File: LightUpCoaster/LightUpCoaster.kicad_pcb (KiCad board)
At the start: 2 copper layers, 53 x 61.3 mm, 54 parts, among them Q101 2N7002, Q102 BSS84, Q103 IRLML6244, Q201 2N2222, Q202 2N2222, Q401 IRLML6244, Q402 IRLML6244, Q403 IRLML6244, Q501 IRLML6244, Q601 IRLML6244, SW102 SW_SPDT, SW103 SW_DIP_x01, U103 CR2032, U104 NE555D, U105 4017

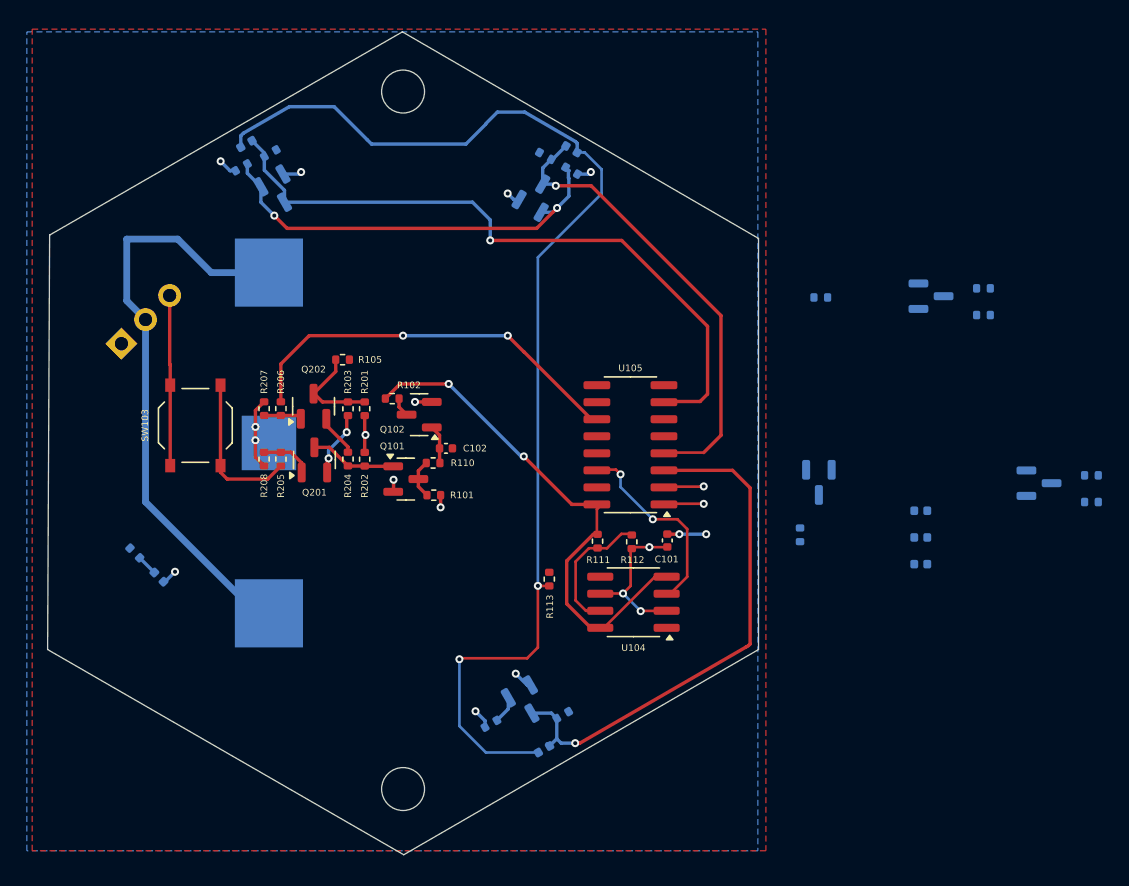
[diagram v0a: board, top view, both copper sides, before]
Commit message: Fixed LED positions
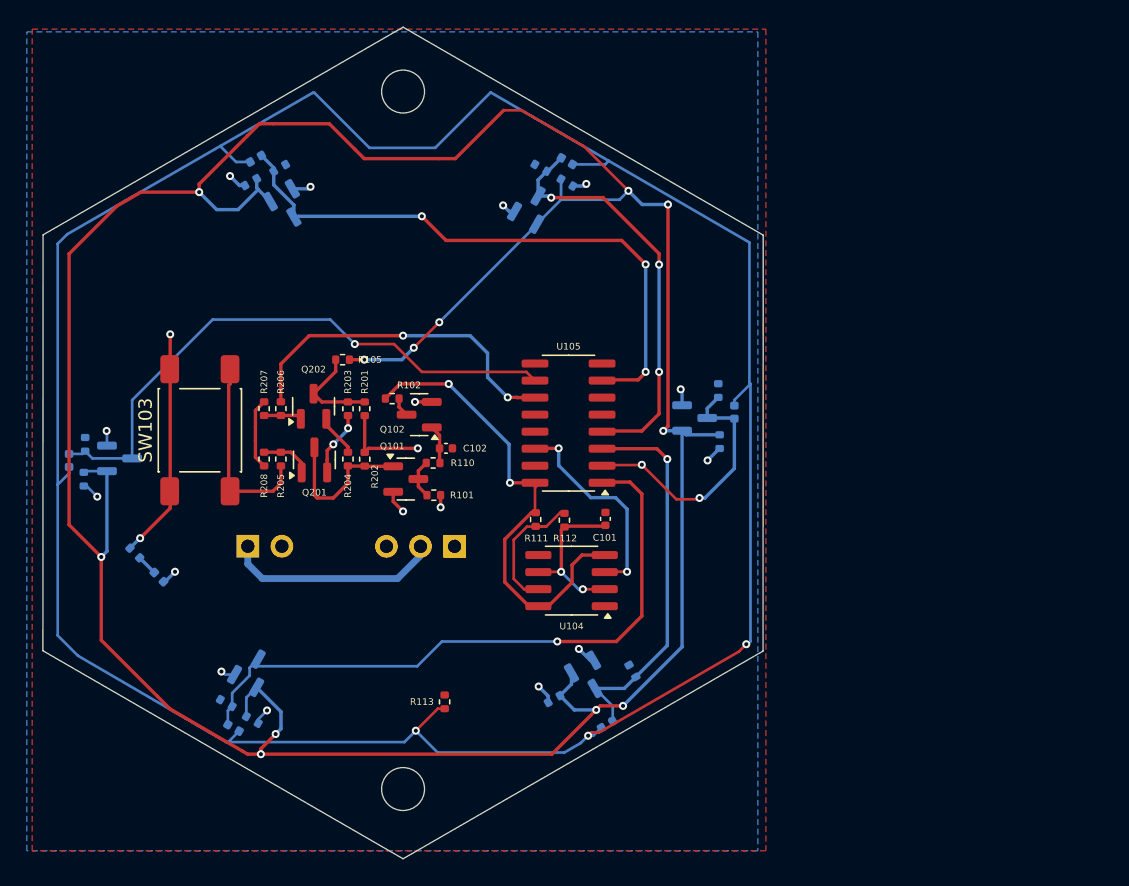
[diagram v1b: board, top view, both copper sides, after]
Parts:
- removed U103: CR2032, Battery_Holder:CR2032-SMD
- added J101: Conn_01x02, Connector_PinHeader_2.54mm:PinHeader_1x02_P2.54mm_Vertical, B.Cu at (138.4, 107.7)
- SW103: footprint Button_Switch_SMD:SW_Push_1P1T_XKB_TS-1187A -> Button_Switch_SMD:SW_Push_1P1T_NO_E-Switch_TL3301NxxxxxG
- moved R403 75.1 mm to (126.2, 102.7), turned to 90 degrees
- moved R404 75.1 mm to (126.3, 100.1), turned to 90 degrees
- moved Q402 68.6 mm to (128.9, 101.2)
- moved R502 64.4 mm to (136.8, 119.4), turned to 150 degrees
- moved D113 64.0 mm to (125.1, 101.3), turned to 90 degrees
- moved R501 62.3 mm to (138.8, 120.6), turned to 150 degrees
- moved Q501 57.8 mm to (138.7, 116.9), turned to 60 degrees
- moved D116 53.7 mm to (137.4, 121.2), turned to 150 degrees
- moved SW102 29.1 mm to (153.8, 107.7), turned to 90 degrees
- moved D115 16.7 mm to (174.7, 97.7), turned to -90 degrees
- moved R113 12.0 mm to (153.1, 119.3)
- moved Q401 10.4 mm to (171.7, 98.1), turned to 0 degrees
- moved R402 10.3 mm to (173.5, 96.1), turned to 90 degrees
- moved R401 9.18 mm to (173.6, 99.9), turned to 90 degrees
- moved R103 6.15 mm to (167.1, 117.0), turned to 120 degrees
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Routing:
- net /O1: track 33.7 -> 228.7 mm, vias 2 -> 12
- net /K: track 88.6 -> 192.2 mm, vias 2 -> 3
- net /Q5: track 2.55 -> 48.4 mm
- net /Q4: track 0.00 -> 43.8 mm, vias 0 -> 1
- net +VBatt: track 44.5 -> 15.4 mm
- net /Q1: track 2.56 -> 19.1 mm, vias 1 -> 2
- net /Q0: track 39.8 -> 29.3 mm
- net +3V: track 17.8 -> 26.2 mm, vias 3 -> 5
- net /Q3: track 50.0 -> 44.4 mm, vias 1 -> 3
- net /SR_Latch/O2: track 6.46 -> 11.3 mm
- net /Q9: track 30.0 -> 25.6 mm
- net GND: track 18.1 -> 22.5 mm, vias 12 -> 14
- net /Q2: track 34.3 -> 30.7 mm, vias 1 -> 3
- net VCC: track 38.7 -> 35.4 mm
- net /SR_Latch/Set: track 11.6 -> 14.3 mm
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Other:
- board size 53 x 61.3 mm -> 53.7 x 62 mm
- board text added: "+3V"
